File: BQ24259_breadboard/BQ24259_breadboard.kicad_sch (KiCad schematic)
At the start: 30 parts, among them J1 USB_C_Receptacle_USB2.0, J2 Power_In, J3 Battery, J4 PWR_Left, J5 PWR_Right, J6 BatTemp, J7 BB_Left, J9 BB_Right, SW1 PWR_Select, U1 BQ24259RGER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

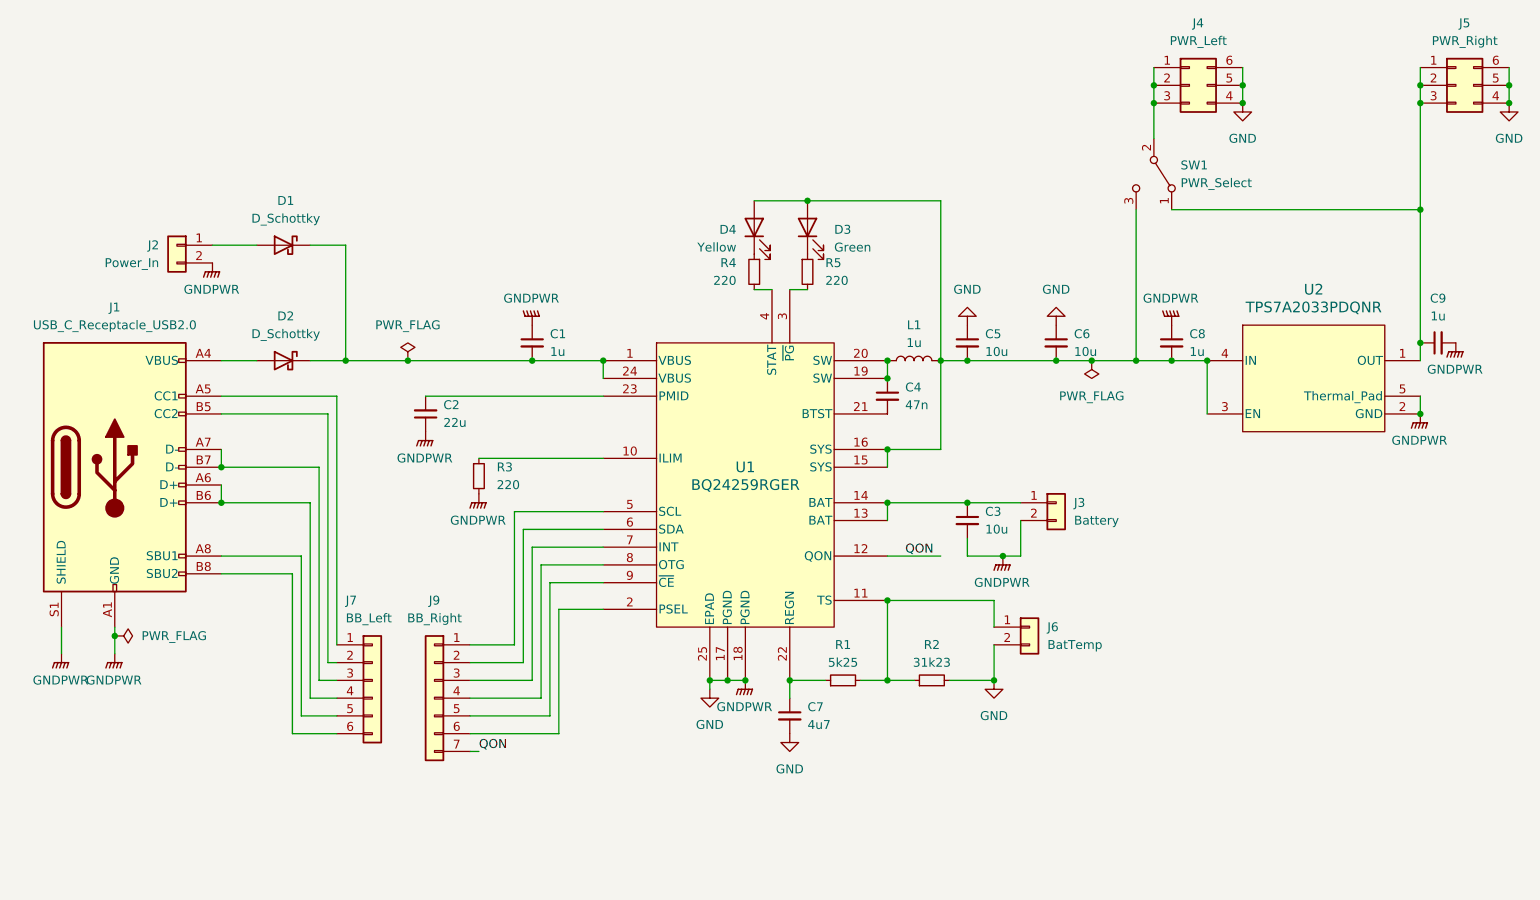
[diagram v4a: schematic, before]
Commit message: Remove power rail connectors
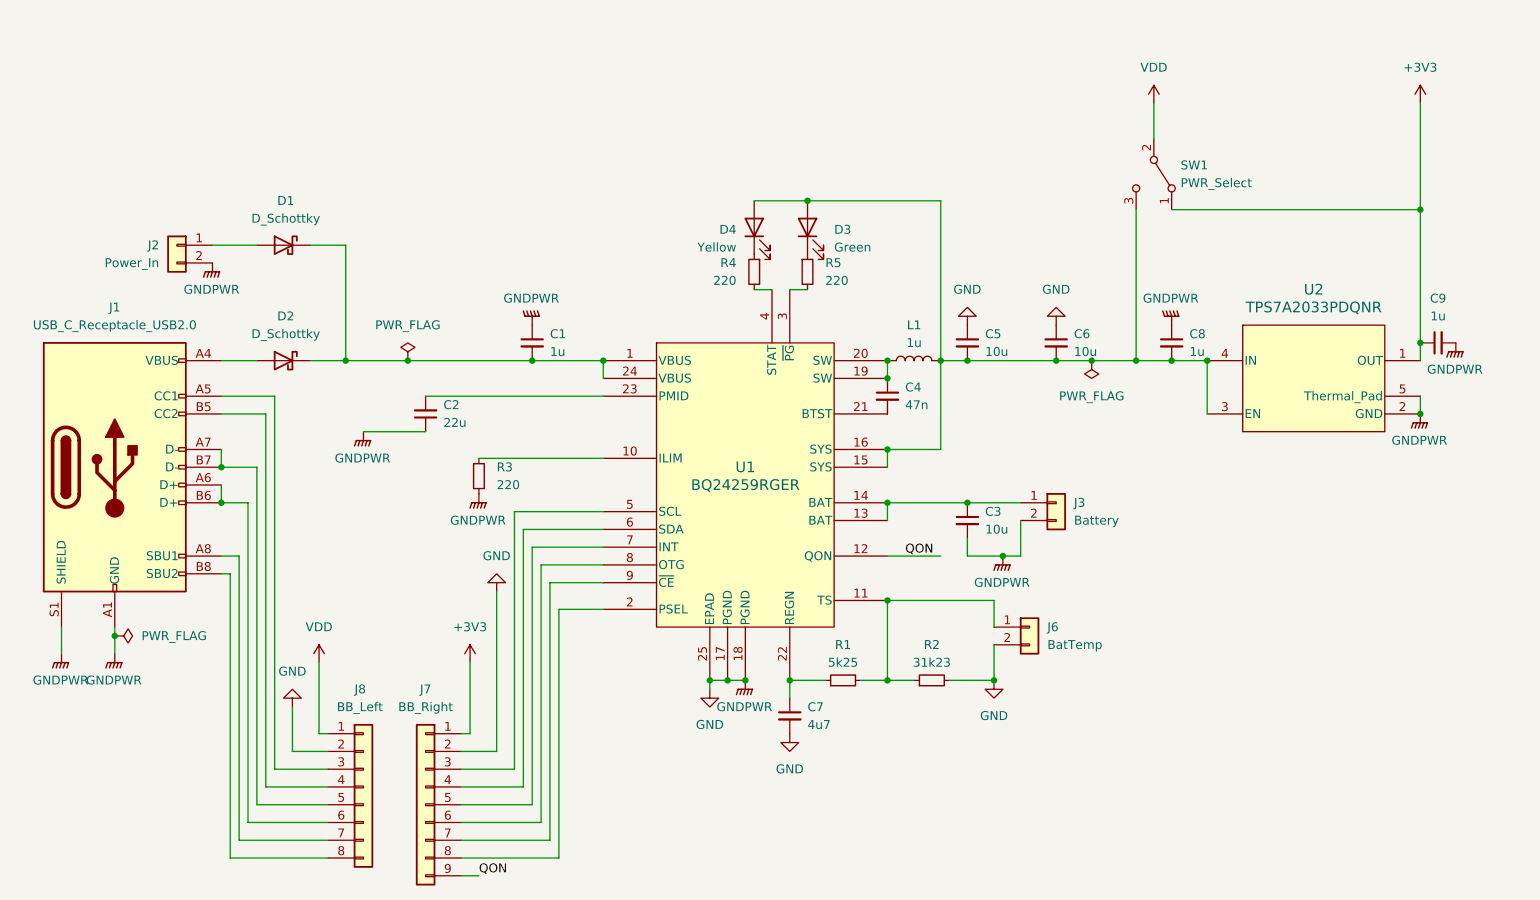
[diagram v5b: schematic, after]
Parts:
- removed J4: PWR_Left, Connector_PinHeader_2.54mm:PinHeader_2x03_P2.54mm_Vertical, symbol Connector_Generic:Conn_02x03_Counter_Clockwise
- removed J5: PWR_Right, Connector_PinHeader_2.54mm:PinHeader_2x03_P2.54mm_Vertical, symbol Connector_Generic:Conn_02x03_Counter_Clockwise
- removed J7: BB_Left, Connector_PinHeader_2.54mm:PinHeader_1x06_P2.54mm_Vertical, symbol Connector_Generic:Conn_01x06
- removed J9: BB_Right, Connector_PinHeader_2.54mm:PinHeader_1x07_P2.54mm_Vertical, symbol Connector_Generic:Conn_01x07
- added J7: BB_Right, Connector_PinHeader_2.54mm:PinHeader_1x09_P2.54mm_Vertical, symbol Connector_Generic:Conn_01x09
- added J8: BB_Left, Connector_PinHeader_2.54mm:PinHeader_1x08_P2.54mm_Vertical, symbol Connector_Generic:Conn_01x08
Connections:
- net GND: now also J7.2 (Pin_2), J8.2 (Pin_2)
- net QON: now also J7.9 (Pin_9)
- net +3V3: now reaches C9.1, SW1.1 (A), U2.1 (OUT)
- net +3V3: now also J7.1 (Pin_1)
- net VDD: now reaches SW1.2 (B)
- net VDD: now also J8.1 (Pin_1)
- net at J1.A5 (CC1): now also J8.3 (Pin_3)
- net at J1.A6 (D+), J1.B6 (D+): now also J8.6 (Pin_6)
- net at J1.A7 (D-), J1.B7 (D-): now also J8.5 (Pin_5)
- net at J1.A8 (SBU1): now also J8.7 (Pin_7)
- net at J1.B5 (CC2): now also J8.4 (Pin_4)
- net at J1.B8 (SBU2): now also J8.8 (Pin_8)
- net at U1.2 (PSEL): now also J7.8 (Pin_8)
- net at U1.5 (SCL): now also J7.3 (Pin_3)
- net at U1.6 (SDA): now also J7.4 (Pin_4)
- net at U1.7 (INT): now also J7.5 (Pin_5)
- net at U1.8 (OTG): now also J7.6 (Pin_6)
- net at U1.9 (~{CE}): now also J7.7 (Pin_7)

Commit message: Routed PCB with a few problems
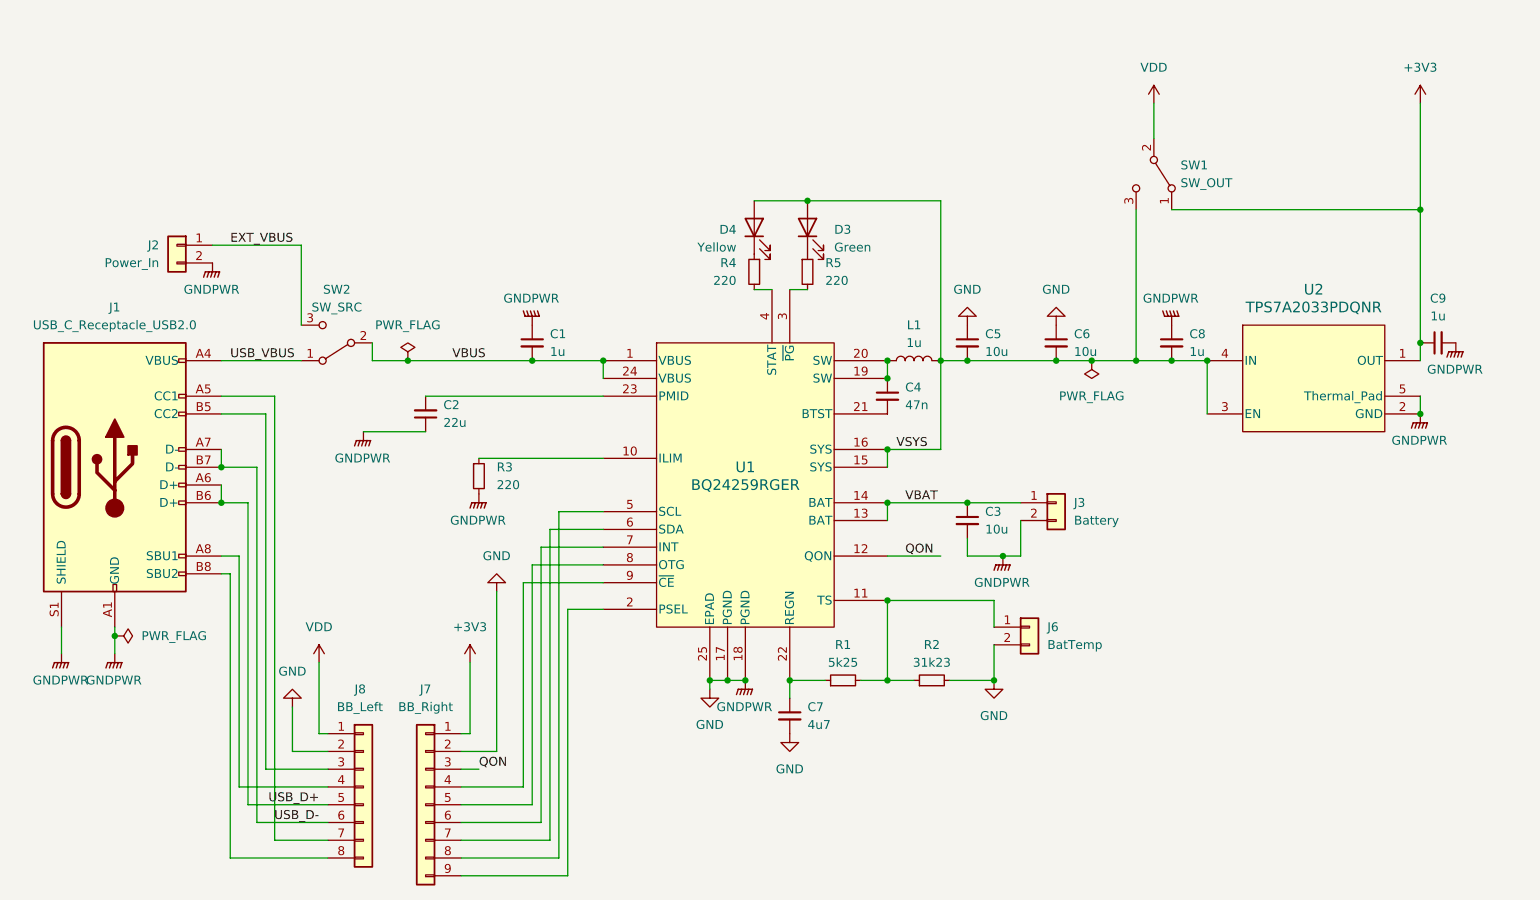
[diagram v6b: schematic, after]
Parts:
- removed D1, D2: D_Schottky, Diode_SMD:D_SMA, symbol Device:D_Schottky
- added SW2: SW_SRC, Connector_PinHeader_2.54mm:PinHeader_1x03_P2.54mm_Vertical, symbol Switch:SW_SPDT
- C1: footprint Connector_JST:JST_PH_B2B-PH-SM4-TB_1x02-1MP_P2.00mm_Vertical -> Capacitor_SMD:C_0603_1608Metric
- SW1: value PWR_Select -> SW_OUT
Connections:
- net QON: now also J7.3 (Pin_3); no longer J7.9 (Pin_9)
- net VSYS: now reaches C5.2, C6.2, C8.2, D3.2 (A), D4.2 (A), L1.2, SW1.3 (C), U1.15 (SYS), U1.16 (SYS), U2.3 (EN), U2.4 (IN)
- net VBUS: now reaches C1.2, U1.1 (VBUS), U1.24 (VBUS)
- net VBUS: now also SW2.2 (B)
- net USB_VBUS: now reaches J1.A4 (VBUS), J1.A9 (VBUS), J1.B4 (VBUS), J1.B9 (VBUS)
- net USB_VBUS: now also SW2.1 (A)
- net VBAT: now reaches C3.1, J3.1 (Pin_1), U1.13 (BAT), U1.14 (BAT)
- net EXT_VBUS: now reaches J2.1 (Pin_1)
- net EXT_VBUS: now also SW2.3 (C)
- net at U1.5 (SCL): now also J7.8 (Pin_8); no longer J7.3 (Pin_3)
- net at J7.4 (Pin_4): now also U1.9 (~{CE}); no longer U1.6 (SDA)
- net at J7.5 (Pin_5): now also U1.8 (OTG); no longer U1.7 (INT)
- net at J7.6 (Pin_6): now also U1.7 (INT); no longer U1.8 (OTG)
- net at J7.7 (Pin_7): now also U1.6 (SDA); no longer U1.9 (~{CE})
- net at U1.2 (PSEL): now also J7.9 (Pin_9); no longer J7.8 (Pin_8)
- net at J1.A5 (CC1): now also J8.7 (Pin_7); no longer J8.3 (Pin_3)
- net USB_D+: now reaches J1.A6 (D+), J1.B6 (D+)
- net USB_D+: now also J8.5 (Pin_5); no longer J8.6 (Pin_6)
- net USB_D-: now reaches J1.A7 (D-), J1.B7 (D-)
- net USB_D-: now also J8.6 (Pin_6); no longer J8.5 (Pin_5)
- net at J1.A8 (SBU1): now also J8.4 (Pin_4); no longer J8.7 (Pin_7)
- net at J1.B5 (CC2): now also J8.3 (Pin_3); no longer J8.4 (Pin_4)
